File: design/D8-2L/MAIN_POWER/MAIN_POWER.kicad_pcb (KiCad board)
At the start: 2 copper layers, 121.8 x 60.5 mm, 17 parts, among them J1 12V INPUT - FLAT SOLDER PADS, J2 JETSON 12V 5A, J3 GMSL 12V / EXCLUSIVE WITH POE, J4 FAN 12V 0.14A, J5 USB BOARD 12V, J6 POE BOARD 12V INPUT

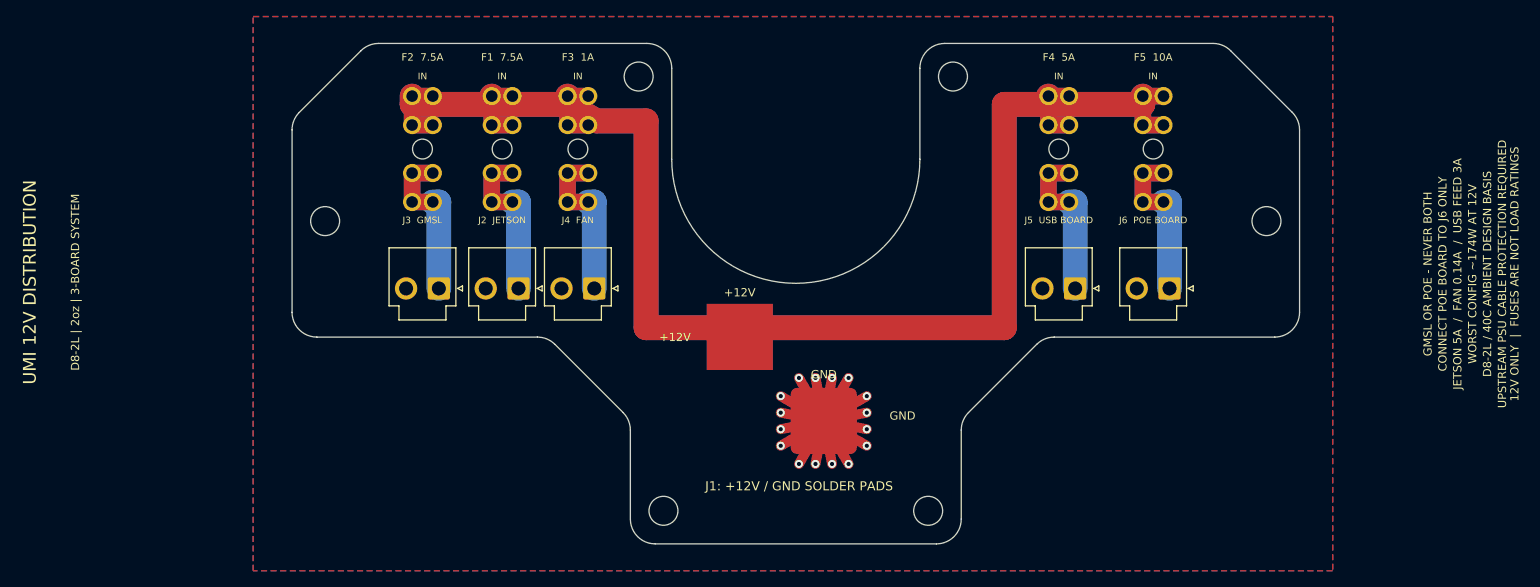
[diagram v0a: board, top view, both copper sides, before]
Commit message: Apply MAIN V3 outline and export FASTON STEP
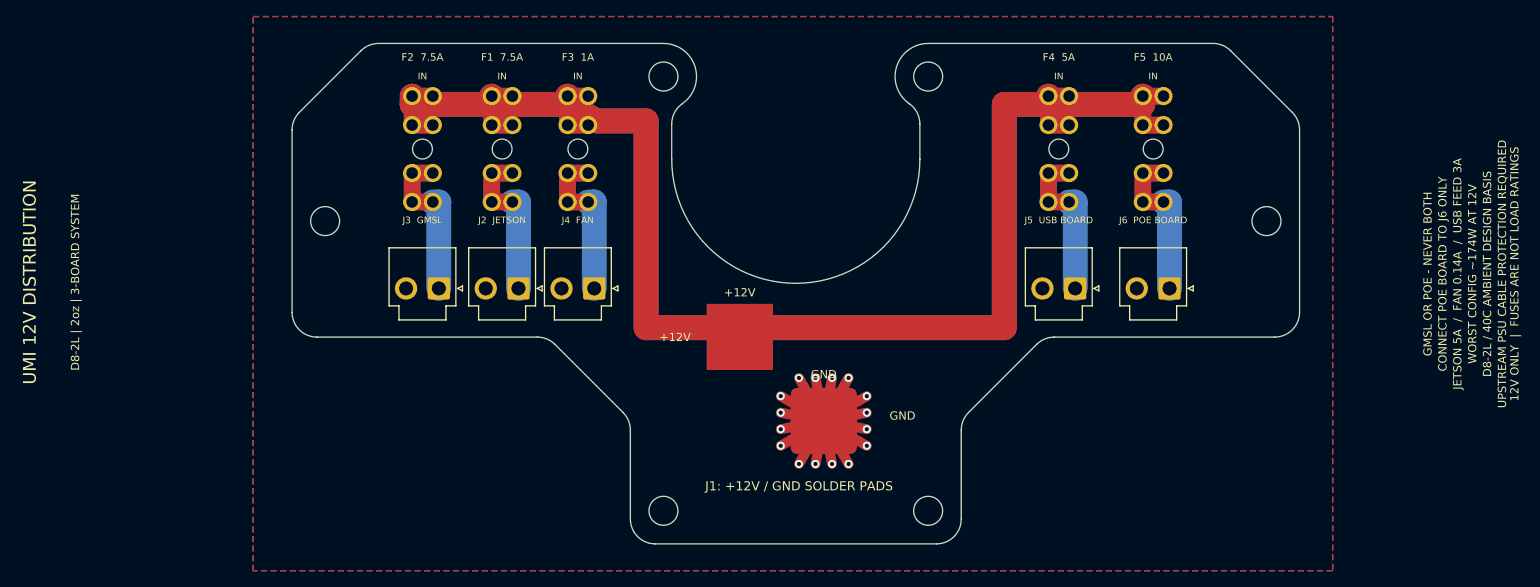
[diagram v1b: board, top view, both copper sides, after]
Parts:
- moved H2 3.00 mm to (123.6, 59.1)
- moved H5 3.00 mm to (155.6, 59.1)
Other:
- outline, holes or cut-outs redrawn
